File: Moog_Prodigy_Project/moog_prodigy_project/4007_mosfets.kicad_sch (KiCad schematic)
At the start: 28 parts, among them Q12 BC327, Q13 BC327, SW10 FINAL DECAY SWITCH, SW9 FINAL DECAY SWITCH, U18 OPA184, U19 OPA184

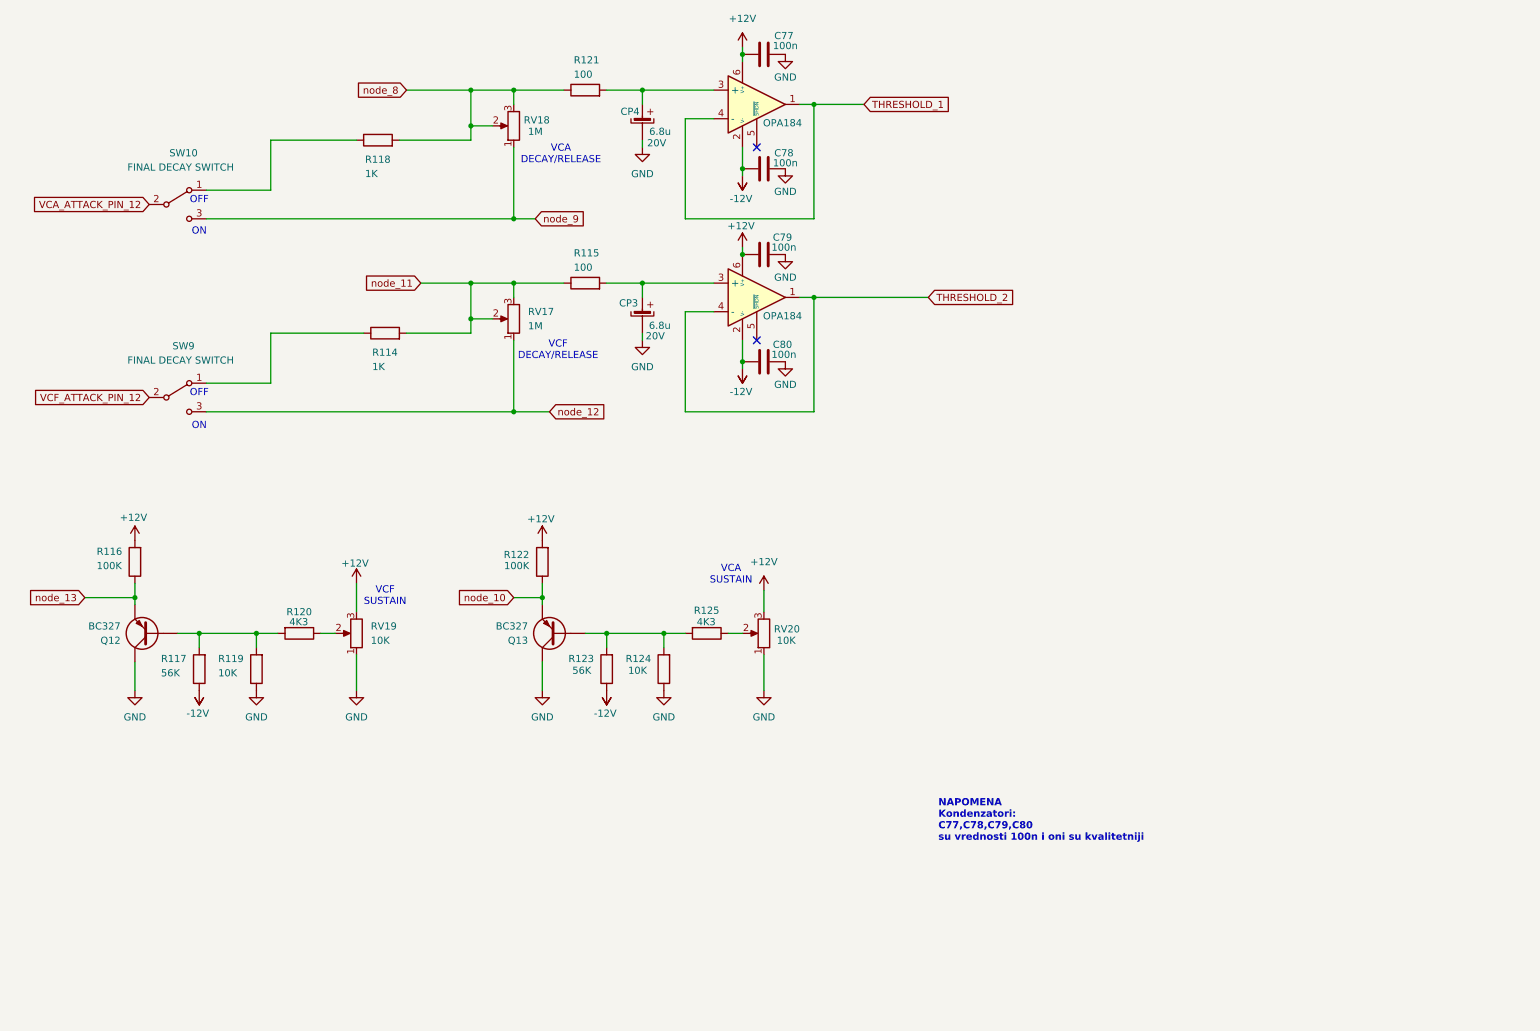
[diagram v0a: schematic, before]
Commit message: Dodao u napomenu za linearne i logaritamske potenciometre, NE555 i sa 4007 semom spojena u jedno, dodati kvalitetni kondenzatori, ostao simbol za 4007 da izenim kao sto je jocke
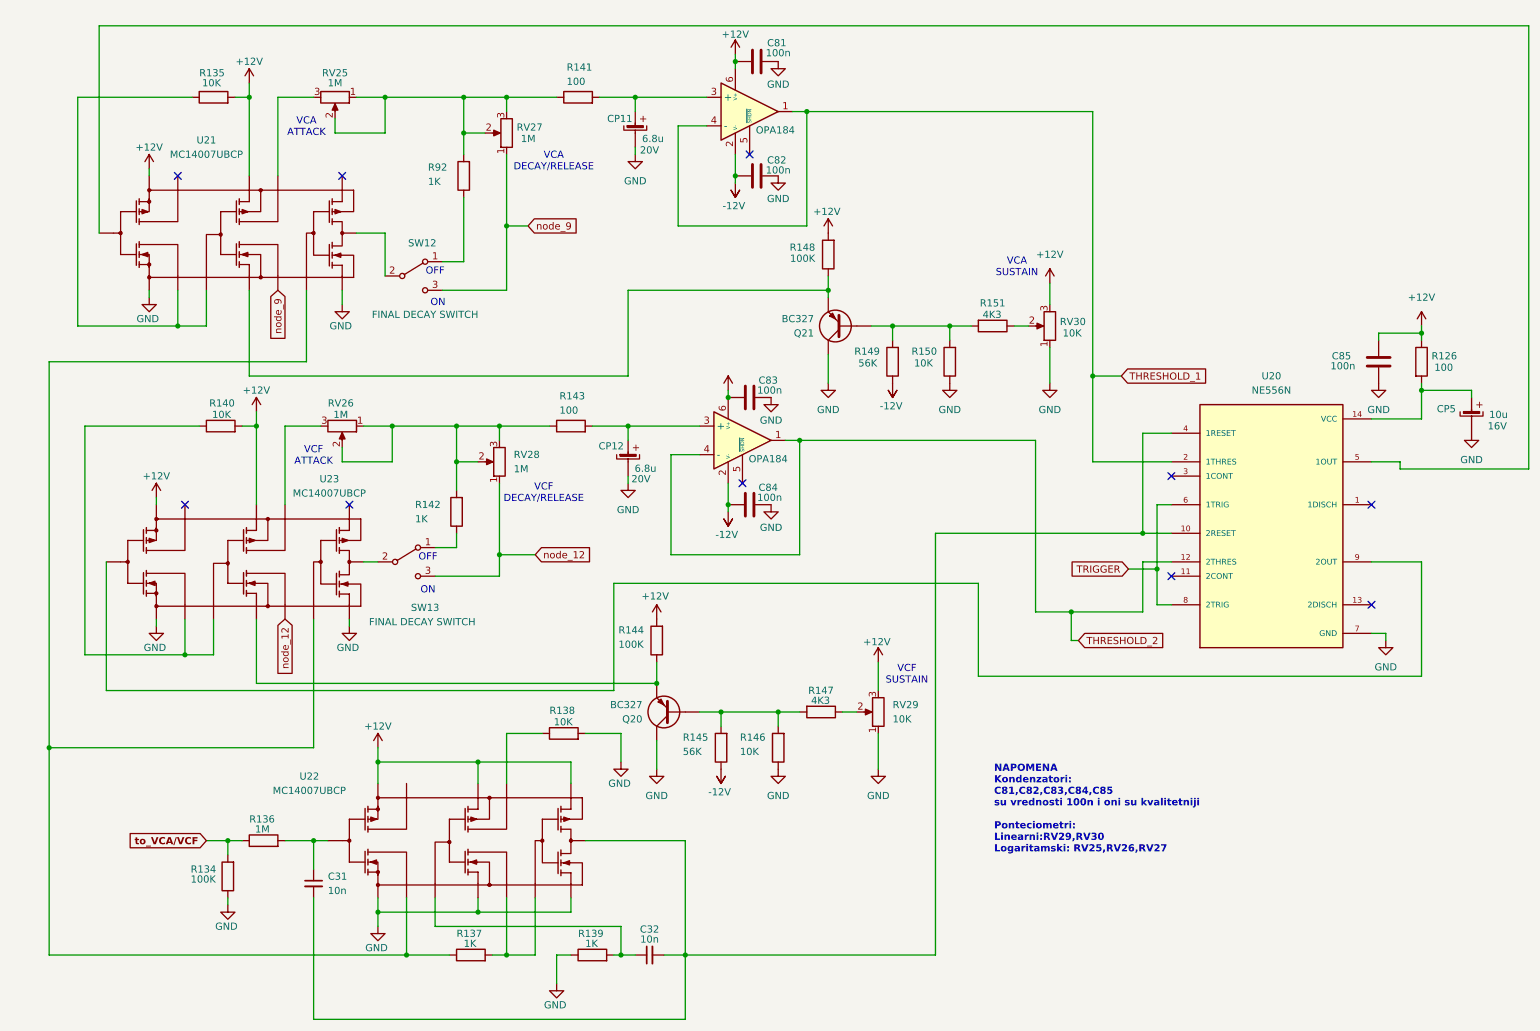
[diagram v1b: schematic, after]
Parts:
- removed C77, C78, C79, C80: 100n, Capacitor_THT:CP_Radial_D5.0mm_P2.50mm, symbol Device:C
- removed CP3, CP4: 6.8u, Capacitor_THT:CP_Radial_D5.0mm_P2.50mm, symbol elektrolitski:elektrolit
- removed Q12, Q13: BC327, Package_TO_SOT_THT:TO-92_Inline, symbol Transistor_BJT:BC556
- removed R114, R118: 1K, Resistor_THT:R_Axial_DIN0207_L6.3mm_D2.5mm_P7.62mm_Horizontal, symbol Device:R
- removed R115, R121: 100, Resistor_THT:R_Axial_DIN0207_L6.3mm_D2.5mm_P7.62mm_Horizontal, symbol Device:R
- removed R116, R122: 100K, Resistor_THT:R_Axial_DIN0207_L6.3mm_D2.5mm_P7.62mm_Horizontal, symbol Device:R
- removed R117, R123: 56K, Resistor_THT:R_Axial_DIN0207_L6.3mm_D2.5mm_P7.62mm_Horizontal, symbol Device:R
- removed R119, R124: 10K, Resistor_THT:R_Axial_DIN0207_L6.3mm_D2.5mm_P7.62mm_Horizontal, symbol Device:R
- removed R120, R125: 4K3, Resistor_THT:R_Axial_DIN0207_L6.3mm_D2.5mm_P7.62mm_Horizontal, symbol Device:R
- removed RV17, RV18: 1M, Potentiometer_THT:Potentiometer_ACP_CA9-V10_Vertical, symbol Device:R_Potentiometer
- removed RV19, RV20: 10K, Potentiometer_THT:Potentiometer_ACP_CA9-V10_Vertical, symbol Device:R_Potentiometer
- removed SW10, SW9: FINAL DECAY SWITCH, ATE1D-2M3-10-Z_1x2:SW_ATE1D-2M3-10-Z, symbol Switch:SW_SPDT
- removed U18, U19: OPA184, Package_DIP:DIP-8_W7.62mm, symbol Amplifier_Operational:OPA310SxDBV
- added C31, C32: 10n, Capacitor_THT:C_Disc_D3.8mm_W2.6mm_P2.50mm, symbol Device:C_Small
- added C81, C82, C83, C84, C85: 100n, Capacitor_THT:CP_Radial_D5.0mm_P2.50mm, symbol Device:C
- added CP11, CP12: 6.8u, Capacitor_THT:CP_Radial_D5.0mm_P2.50mm, symbol elektrolitski:elektrolit
- added CP5: 10u, Capacitor_THT:CP_Radial_D5.0mm_P2.50mm, symbol elektrolitski:elektrolit
- added Q20, Q21: BC327, Package_TO_SOT_THT:TO-92_Inline, symbol Transistor_BJT:BC556
- added R126, R141, R143: 100, Resistor_THT:R_Axial_DIN0207_L6.3mm_D2.5mm_P7.62mm_Horizontal, symbol Device:R
- added R134, R144, R148: 100K, Resistor_THT:R_Axial_DIN0207_L6.3mm_D2.5mm_P7.62mm_Horizontal, symbol Device:R
- added R135, R138, R140, R146, R150: 10K, Resistor_THT:R_Axial_DIN0207_L6.3mm_D2.5mm_P7.62mm_Horizontal, symbol Device:R
- added R136: 1M, Resistor_THT:R_Axial_DIN0207_L6.3mm_D2.5mm_P7.62mm_Horizontal, symbol Device:R
- added R137, R139, R142, R92: 1K, Resistor_THT:R_Axial_DIN0207_L6.3mm_D2.5mm_P7.62mm_Horizontal, symbol Device:R
- added R145, R149: 56K, Resistor_THT:R_Axial_DIN0207_L6.3mm_D2.5mm_P7.62mm_Horizontal, symbol Device:R
- added R147, R151: 4K3, Resistor_THT:R_Axial_DIN0207_L6.3mm_D2.5mm_P7.62mm_Horizontal, symbol Device:R
- added RV25, RV26, RV27, RV28: 1M, Potentiometer_THT:Potentiometer_ACP_CA9-V10_Vertical, symbol Device:R_Potentiometer
- added RV29, RV30: 10K, Potentiometer_THT:Potentiometer_ACP_CA9-V10_Vertical, symbol Device:R_Potentiometer
- added SW12, SW13: FINAL DECAY SWITCH, ATE1D-2M3-10-Z_1x2:SW_ATE1D-2M3-10-Z, symbol Switch:SW_SPDT
- added U20: NE556N, NE556N:DIP794W45P254L1930H508Q14, symbol NE556N:NE556N
- added U21, U22, U23: MC14007UBCP, Package_DIP:DIP-14_W7.62mm_Socket, symbol MC14007UBCP:MC14007UBCP
- added U26, U27: OPA184, Package_DIP:DIP-8_W7.62mm, symbol Amplifier_Operational:OPA310SxDBV
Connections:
- net +12V: now also C81.2, C83.2, C85.1, R126.1, R135.2, R140.2, R144.2, R148.2, RV29.3, RV30.3, U21., U22., U23., U26.6 (V+), U27.6 (V+)
- net -12V: now also C82.2, C84.2, R145.1, R149.1, U26.2 (V-), U27.2 (V-)
- net GND: now also C81.1, C82.1, C83.1, C84.1, C85.2, CP11., CP12., CP5., Q20. (E), Q21. (E), R134.1, R138.2, R139.1, R146.1, R150.1, RV29.1, RV30.1, U20.7 (GND), U21., U22., U23.
- net THRESHOLD_1: now also U20.2 (1THRES), U26.1, U26.4 (-)
- net THRESHOLD_2: now also U20.12 (2THRES), U27.1, U27.4 (-)
- net node_12: now also RV28.1, SW13.3 (C), U23.
- net node_9: now also RV27.1, SW12.3 (C), U21.
- new net: Q21. (E), R149.2, R150.2, R151.2
- new net: R138.1, U22.
- new net: CP5., R126.2, U20.14 (VCC)
- new net: Q20. (E), R145.2, R146.2, R147.2
- new net: Q20. (E), R144.1, U23.
- new net: Q21. (E), R148.1, U21.
- new net: C32.1, R139.2, U22.
- new net: CP11., R141.2, U26.3 (+)
- new net: R137.1, U21., U22., U23.
- new net: R137.2, U22.
- new net: C31.1, R136.2, U22.
- new net: C31.2, C32.2, U20.10 (2RESET), U20.4 (1RESET), U22.
- new net: R140.1, U23.
- new net: R142.2, R143.1, RV26.1, RV26.2, RV28.2, RV28.3
- new net: RV26.3, U23.
- new net: R141.1, R92.2, RV25.1, RV25.2, RV27.2, RV27.3
- new net: CP12., R143.2, U27.3 (+)
- new net: R92.1, SW12.1 (A)
- new net: R135.1, U21.
- new net: RV25.3, U21.
- new net: U20.5 (1OUT), U21.
- new net: SW12.2 (B), U21.
- new net: R151.1, RV30.2
- new net: R147.1, RV29.2
- new net: R142.1, SW13.1 (A)
- new net: U20.9 (2OUT), U23.
- new net: SW13.2 (B), U23.
- new net TRIGGER: U20.6 (1TRIG), U20.8 (2TRIG)
- new net to_VCA/VCF: R134.2, R136.1
- no-connect marks 2 -> 10
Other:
- note added: "NAPOMENA Kondenzatori: C81,C82,C83,C84,C85 su vrednosti 100n i oni su kvalitetniji Ponteciometri: Linearni:RV29,RV30 Logaritamski: RV25,RV26,RV27"
- note added: "VCA ATTACK"
- note added: "VCF ATTACK"
- note removed: "NAPOMENA Kondenzatori: C77,C78,C79,C80 su vrednosti 100n i oni su kvalitetniji"
- title: (none) -> VCA, VCF i NE555 dualni brojač

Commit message: nova schema 4007
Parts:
- removed R140: 10K, Resistor_THT:R_Axial_DIN0207_L6.3mm_D2.5mm_P7.62mm_Horizontal, symbol Device:R
- added C79, C80, C86: 100n, Capacitor_THT:C_Disc_D3.8mm_W2.6mm_P2.50mm, symbol Device:C_Small
- added R114: 10K, Resistor_THT:R_Axial_DIN0207_L6.3mm_D2.5mm_P7.62mm_Horizontal, symbol Device:R
- R137: value 1K -> 10K
- R139: value 1K -> 100K
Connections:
- net +12V: now also C79.2, C80.2, C86.2, R114.2
- net GND: now also R139.2, C79.1, C80.1, C86.1; no longer R139.1
- net TRIGGER: now also R138.1, U22.
- net node_12: no longer RV28.1, SW13.3 (C), U23.
- net at C31.2, U20.10 (2RESET), U20.4 (1RESET): no longer C32.2, U22.
- net node_9: no longer names the net of RV27.1, SW12.3 (C), U21.
- new net: Q20. (E), R144.1, U23.
- new net: Q21. (E), R148.1, U21.
- new net: C32.2, R139.1, U22.
- new net: R137.1, U21., U22., U23.
- new net: C32.1, U22.
- new net: RV28.1, SW13.3 (C), U23.
- new net: R114.1, U23.
- no-connect marks 10 -> 12
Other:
- note added: "IC3"
- note added: "IC3_1"
- note added: "IC3_2"
- note added: "IC3_3"
- note added: "IC3_4"
- note added: "IC3_5"
- note added: "IC3_6"
- note added: "IC4"
- note added: "IC4_1"
- note added: "IC4_2"
- note added: "IC4_3"
- note added: "IC4_4"
- note added: "IC4_5"
- note added: "IC4_6"
- note added: "IC5"
- note added: "IC5_1"
- note added: "IC5_2"
- note added: "IC5_3"
- note added: "IC5_4"
- note added: "IC5_5"
- note added: "IC5_6"
- note added: "NAPOMENA Kondenzatori: C79,C80,C81,C82,C83,C84,C85 su vrednosti 100n i oni su kvalitetniji Ponteciometri: Linearni:RV29,RV30 Logaritamski: RV25,RV26,RV27"
- note removed: "NAPOMENA Kondenzatori: C81,C82,C83,C84,C85 su vrednosti 100n i oni su kvalitetniji Ponteciometri: Linearni:RV29,RV30 Logaritamski: RV25,RV26,RV27"
- moved on the sheet: C31, C32, R134, R135, R136, R137, R138, R139, R142, R92, RV25, RV26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

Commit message: MOOG prodigy final 03.07.2026
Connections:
- new net: Q20. (E), R144.1, U23.
- new net: Q21. (E), R148.1, U21.
- new net: R137.1, U21., U22., U23.
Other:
- note added: "NAPOMENA 1 Kondenzatori: C79,C80,C81,C82,C83,C84,C85 su vrednosti 100n i oni su kvalitetniji Ponteciometri: Linearni:RV29,RV30 Logaritamski: RV25,RV26,RV27"
- note added: "NAPOMENA 2 Otpornici cija je vrednost: 63K4, 18K2, 4K75, 6K81, 51M, 2.4M su otpornici iz E96 serije (1%) Ostali orpotnici su iz serije E24 (5%)"
- note removed: "NAPOMENA Kondenzatori: C79,C80,C81,C82,C83,C84,C85 su vrednosti 100n i oni su kvalitetniji Ponteciometri: Linearni:RV29,RV30 Logaritamski: RV25,RV26,RV27"
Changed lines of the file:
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@@
 		)
 	)
-	(text "NAPOMENA\nKondenzatori:\nC79,C80,C81,C82,C83,C84,C85\nsu vrednosti 100n i oni su kvalitetniji\n\nPonteciometri:\nLinearni:RV29,RV30\nLogaritamski: RV25,RV26,RV27"
+	(text "NAPOMENA 1\nKondenzatori:\nC79,C80,C81,C82,C83,C84,C85\nsu vrednosti 100n i oni su kvalitetniji\n\nPonteciometri:\nLinearni:RV29,RV30\nLogaritamski: RV25,RV26,RV27"
 		(exclude_from_sim no)
 		(at 186.944 156.972 0)
@@
 		)
 	)
+	(text "NAPOMENA 2\nOtpornici cija je vrednost:\n63K4, 18K2, 4K75, 6K81, 51M, 2.4M\nsu otpornici iz E96 serije (1%)\nOstali orpotnici su iz serije E24 (5%)"
+		(exclude_from_sim no)
+		(at 227.076 153.924 0)
+		(effects
+			(font
+				(size 1.27 1.27)
+				(thickness 0.254)
+				(bold yes)
+			)
+			(justify left)
+		)
+	)
